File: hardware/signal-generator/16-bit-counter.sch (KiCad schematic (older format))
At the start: 8 parts, among them U1 74HC04, U13 74HC4040, U14 74HC4040, U2 74HC08, U3 74HC08, U4 74HC30

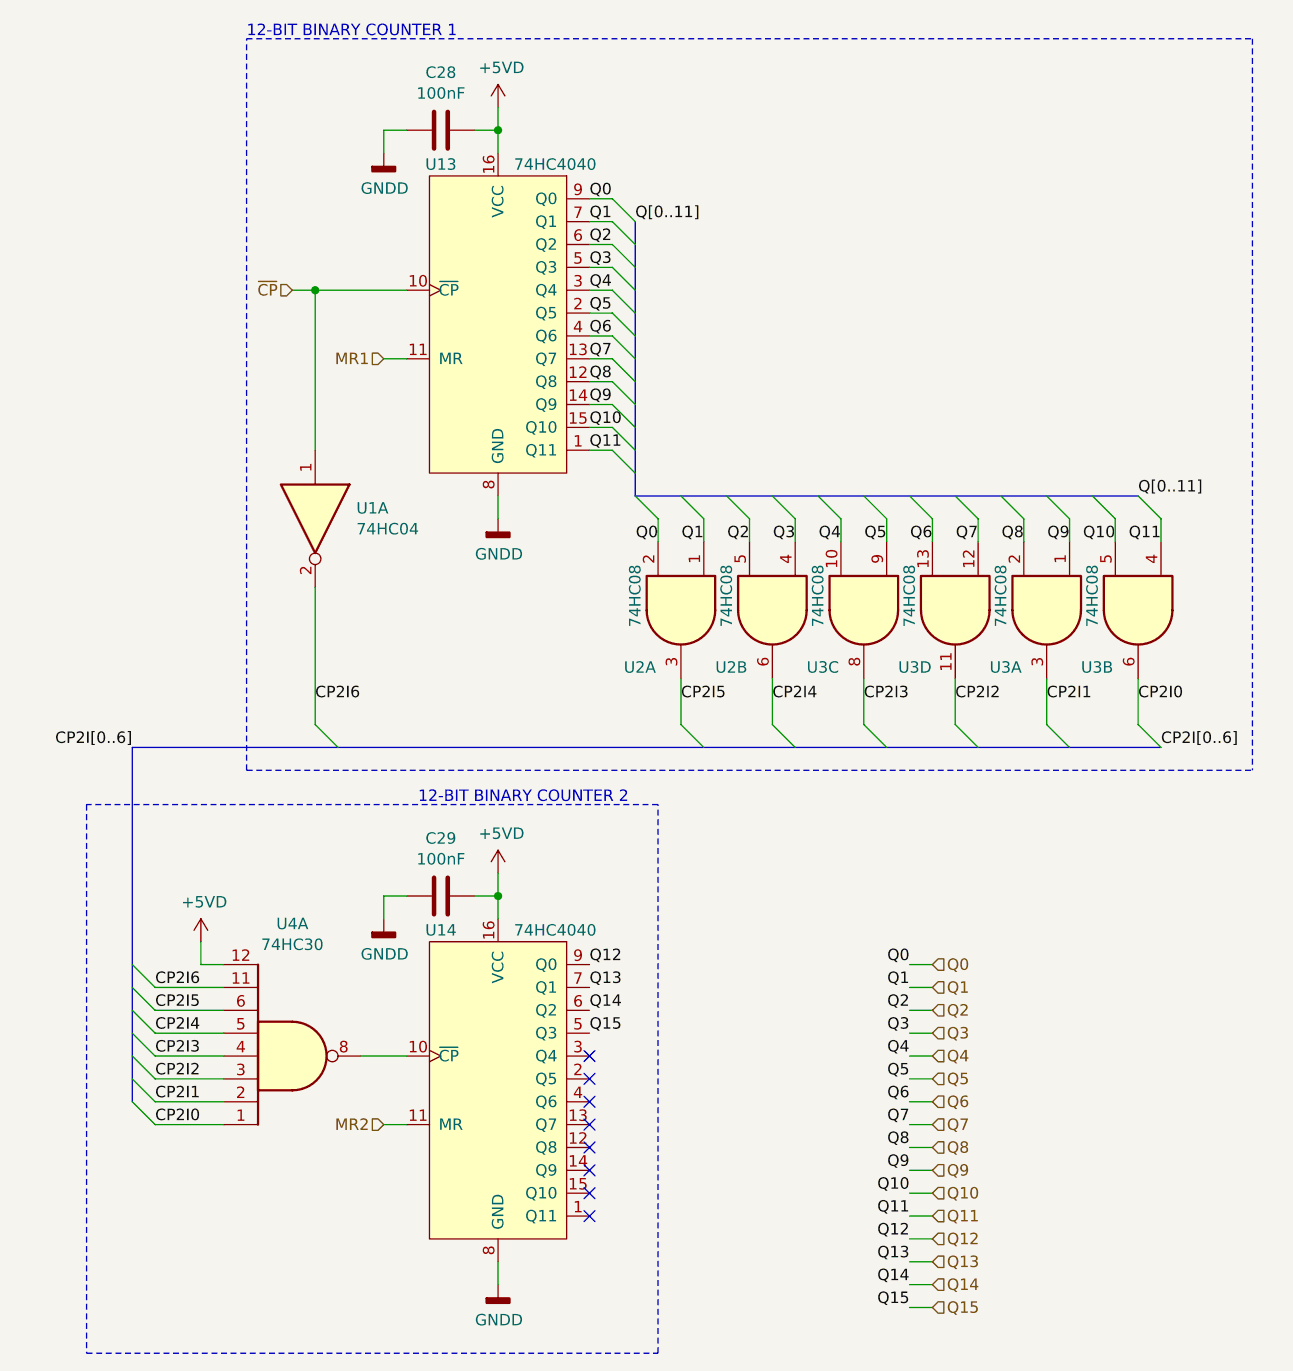
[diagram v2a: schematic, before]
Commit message: [Signal Generator] Complete DDS system layout and routing
All components of the DDS system, as well as their supporting parts, are
laid out compactly on the board.
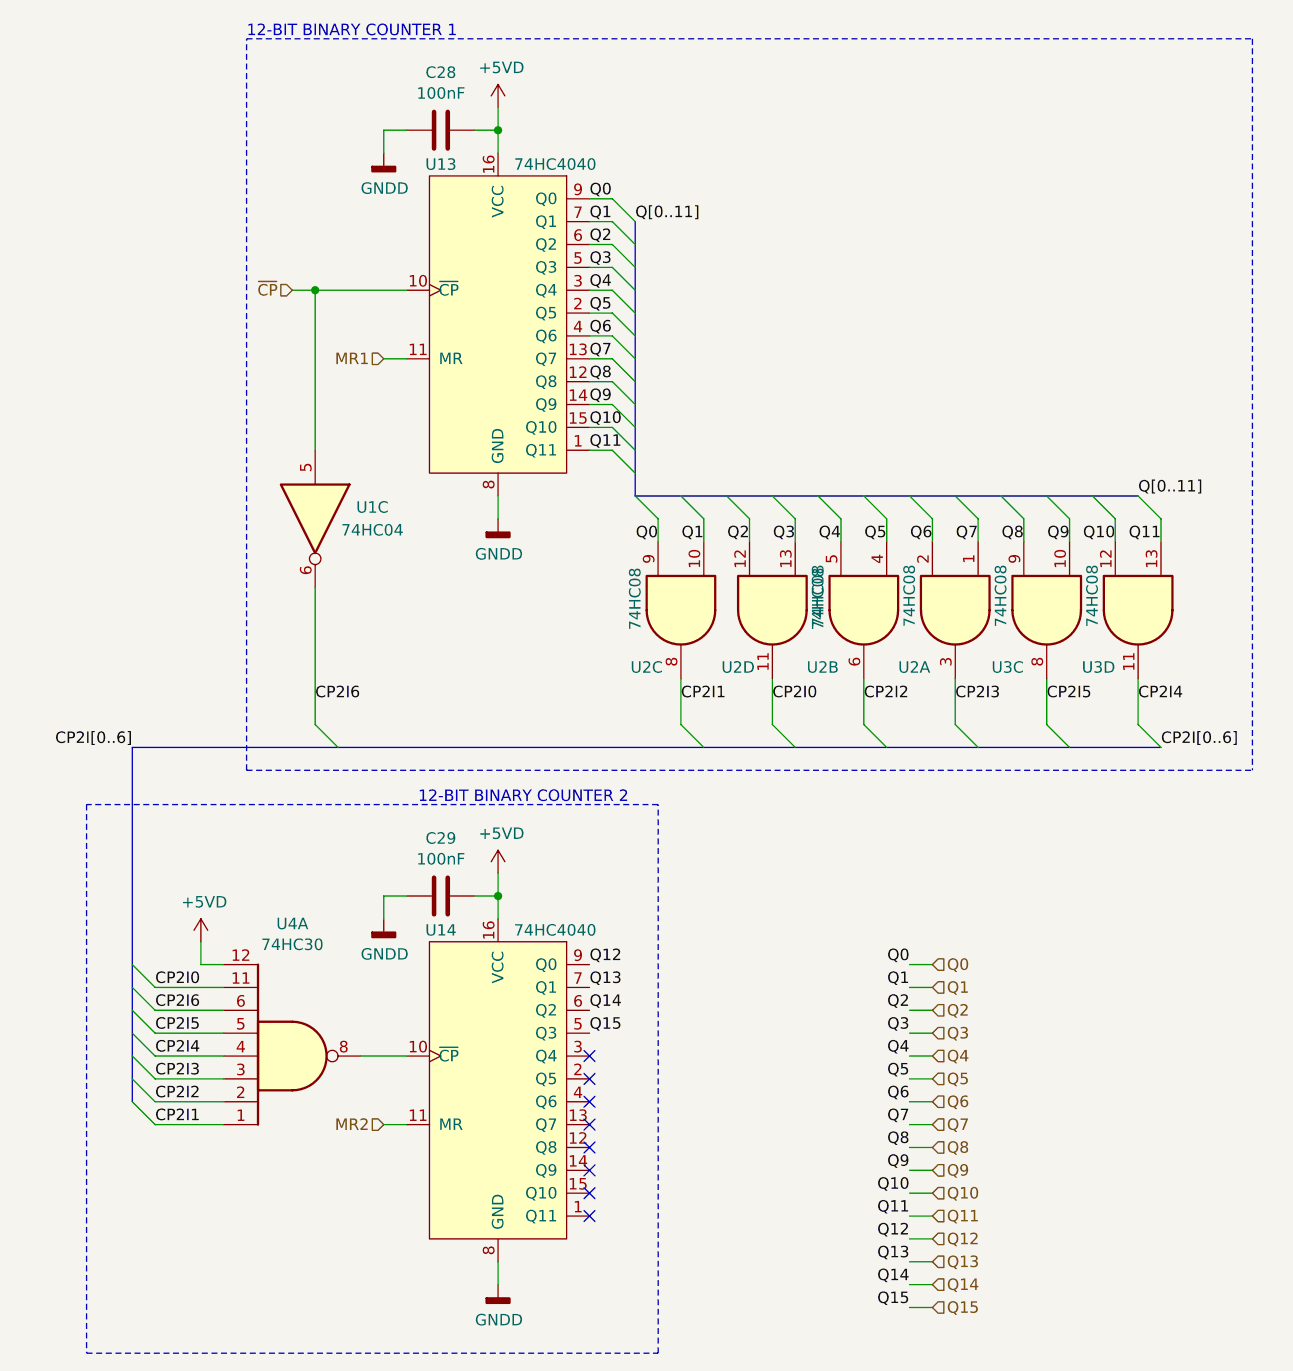
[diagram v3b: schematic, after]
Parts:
- removed U1: 74HC04, Housings_SOIC:SOIC-14_3.9x8.7mm_Pitch1.27mm, symbol 74xx:74HC04
- removed unit 1 of U3
- removed unit 2 of U3
- added U1: 74HC04, Housings_SOIC:SOIC-14_3.9x8.7mm_Pitch1.27mm, symbol 74xx:74HC04
- added unit 4 of U2
- added unit 3 of U2
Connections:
- net CP2I0: now also U4.11, U2.11; no longer U4.1
- net CP2I1: now also U4.1, U2.8; no longer U4.2
- net CP2I2: now also U2.6, U4.2; no longer U3.11, U4.3
- net CP2I3: now also U2.3, U4.3; no longer U3.8, U4.4
- net CP2I4: now also U3.11, U4.4; no longer U2.6, U4.5
- net CP2I5: now also U3.8, U4.5; no longer U2.3, U4.6
- net CP2I6: now also U4.6, U1.6; no longer U4.11
- net Q0: now also U2.9; no longer U2.2
- net Q1: now also U2.10; no longer U2.1
- net Q10: now also U3.12
- net Q11: now also U3.13
- net Q2: now also U2.12; no longer U2.5
- net Q3: now also U2.13; no longer U2.4
- net Q4: now also U2.5; no longer U3.10
- net Q5: now also U2.4; no longer U3.9
- net Q6: now also U2.2; no longer U3.13
- net Q7: now also U2.1; no longer U3.12
- net Q8: now also U3.9
- net Q9: now also U3.10
- net ~CP: now also U1.5
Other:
- moved on the sheet: U2A, U2B, U3C, U3D
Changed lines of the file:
@@
 Sheet 3 5
 Title "Digital Function Generator v2 - DDS 16-bit counter"
-Date "2019-12-02"
+Date "2019-12-26"
 Rev "1"
 Comp "Petar Nikolov"
@@
 Text HLabel 3750 5600 0    50   Input ~ 0
 MR2
+Text Label 2750 5000 0    50   ~ 0
+CP2I0
 Text Label 2750 5600 0    50   ~ 0
-CP2I0
+CP2I1
 Text Label 2750 5500 0    50   ~ 0
-CP2I1
+CP2I2
 Text Label 2750 5400 0    50   ~ 0
-CP2I2
+CP2I3
 Text Label 2750 5300 0    50   ~ 0
-CP2I3
+CP2I4
 Text Label 2750 5200 0    50   ~ 0
-CP2I4
+CP2I5
 Text Label 2750 5100 0    50   ~ 0
-CP2I5
-Text Label 2750 5000 0    50   ~ 0
 CP2I6
 Text Label 2650 3950 2    50   ~ 0
 CP2I[0..6]
+Text Label 5450 3750 0    50   ~ 0
+CP2I0
+Text Label 5050 3750 0    50   ~ 0
+CP2I1
+Text Label 5850 3750 0    50   ~ 0
+CP2I2
+Text Label 6250 3750 0    50   ~ 0
+CP2I3
 Text Label 7050 3750 0    50   ~ 0
-CP2I0
+CP2I4
 Text Label 6650 3750 0    50   ~ 0
-CP2I1
-Text Label 6250 3750 0    50   ~ 0
-CP2I2
-Text Label 5850 3750 0    50   ~ 0
-CP2I3
-Text Label 5450 3750 0    50   ~ 0
-CP2I4
-Text Label 5050 3750 0    50   ~ 0
 CP2I5
 Text Label 3450 3750 0    50   ~ 0
@@
 Text Notes 3900 4200 0    50   ~ 0
 12-BIT BINARY COUNTER 2
-$Comp
-L 74xx:74HC04 U1
-U 1 1 5DBD607E
-P 3450 2950
-F 0 "U1" V 3404 3130 50  0000 L CNN
-F 1 "74HC04" V 3495 3130 50  0000 L CNN
-F 2 "Housings_SOIC:SOIC-14_3.9x8.7mm_Pitch1.27mm" H 3450 2950 50  0001 C CNN
-F 3 "https://assets.nexperia.com/documents/data-sheet/74HC_HCT04.pdf" H 3450 2950 50  0001 C CNN
-	1    3450 2950
-	0    1    1    0
-$EndComp
 Wire Notes Line
 	3150 4050 3150 850
@@
 $Comp
 L ulib_MY_74xx:74HC08 U2
-U 1 1 5DDE88D1
-P 5050 3350
-F 0 "U2" V 5300 3100 50  0000 L CNN
-F 1 "74HC08" H 4850 3150 50  0000 L CNN
-F 2 "Housings_SOIC:SOIC-14_3.9x8.7mm_Pitch1.27mm" H 5050 3300 50  0001 C CNN
-F 3 "https://assets.nexperia.com/documents/data-sheet/74HC_HCT08.pdf" H 5050 3400 50  0001 C CNN
-	1    5050 3350
-	0    1    1    0
-$EndComp
-$Comp
-L ulib_MY_74xx:74HC08 U2
 U 2 1 5DDE89F7
-P 5450 3350
-F 0 "U2" V 5700 3100 50  0000 L CNN
-F 1 "74HC08" H 5250 3150 50  0000 L CNN
-F 2 "Housings_SOIC:SOIC-14_3.9x8.7mm_Pitch1.27mm" H 5450 3300 50  0001 C CNN
-F 3 "https://assets.nexperia.com/documents/data-sheet/74HC_HCT08.pdf" H 5450 3400 50  0001 C CNN
-	2    5450 3350
-	0    1    1    0
-$EndComp
-$Comp
-L ulib_MY_74xx:74HC08 U3
-U 3 1 5DDE8B26
 P 5850 3350
-F 0 "U3" V 6100 3100 50  0000 L CNN
+F 0 "U2" V 6100 3100 50  0000 L CNN
 F 1 "74HC08" H 5650 3150 50  0000 L CNN
 F 2 "Housings_SOIC:SOIC-14_3.9x8.7mm_Pitch1.27mm" H 5850 3300 50  0001 C CNN
 F 3 "https://assets.nexperia.com/documents/data-sheet/74HC_HCT08.pdf" H 5850 3400 50  0001 C CNN
-	3    5850 3350
+	2    5850 3350
 	0    1    1    0
+$EndComp
+$Comp
+L ulib_MY_74xx:74HC08 U3
+U 3 1 5DDE8B26
+P 6650 3350
+F 0 "U3" V 6900 3450 50  0000 L CNN
+F 1 "74HC08" H 6450 3550 50  0000 L CNN
+F 2 "Housings_SOIC:SOIC-14_3.9x8.7mm_Pitch1.27mm" H 6650 3300 50  0001 C CNN
+F 3 "https://assets.nexperia.com/documents/data-sheet/74HC_HCT08.pdf" H 6650 3400 50  0001 C CNN
+	3    6650 3350
+	0    -1   1    0
 $EndComp
 $Comp
 L ulib_MY_74xx:74HC08 U3
 U 4 1 5DDE8C64
+P 7050 3350
+F 0 "U3" V 7300 3450 50  0000 L CNN
+F 1 "74HC08" H 6850 3550 50  0000 L CNN
+F 2 "Housings_SOIC:SOIC-14_3.9x8.7mm_Pitch1.27mm" H 7050 3300 50  0001 C CNN
+F 3 "https://assets.nexperia.com/documents/data-sheet/74HC_HCT08.pdf" H 7050 3400 50  0001 C CNN
+	4    7050 3350
+	0    -1   1    0
+$EndComp
+$Comp
+L ulib_MY_74xx:74HC08 U2
+U 4 1 5E0FAF21
+P 5450 3350
+AR Path="/5DB72CF6/5DBBB708/5E0FAF21" Ref="U2"  Part="4"
+AR Path="/5DE65B3D/5E0FAF21" Ref="U?"  Part="4"
+AR Path="/5E0FAF21" Ref="U?"  Part="4"
+F 0 "U2" V 5700 3500 50  0000 C CNN
+F 1 "74HC08" H 5400 3150 50  0000 C CNN
+F 2 "Housings_SOIC:SOIC-14_3.9x8.7mm_Pitch1.27mm" H 5450 3300 50  0001 C CNN
+F 3 "https://assets.nexperia.com/documents/data-sheet/74HC_HCT08.pdf" H 5450 3400 50  0001 C CNN
+	4    5450 3350
+	0    -1   1    0
+$EndComp
+$Comp
+L ulib_MY_74xx:74HC08 U2
+U 3 1 5E137EE3
+P 5050 3350
+AR Path="/5DB72CF6/5DBBB708/5E137EE3" Ref="U2"  Part="3"
+AR Path="/5DE65B3D/5E137EE3" Ref="U?"  Part="3"
+AR Path="/5E137EE3" Ref="U?"  Part="3"
+F 0 "U2" V 5300 3500 50  0000 C CNN
+F 1 "74HC08" H 5000 3550 50  0000 C CNN
+F 2 "Housings_SOIC:SOIC-14_3.9x8.7mm_Pitch1.27mm" H 5050 3300 50  0001 C CNN
+F 3 "https://assets.nexperia.com/documents/data-sheet/74HC_HCT08.pdf" H 5050 3400 50  0001 C CNN
+	3    5050 3350
+	0    -1   1    0
+$EndComp
+$Comp
+L ulib_MY_74xx:74HC08 U2
+U 1 1 5DDE88D1
 P 6250 3350
-F 0 "U3" V 6500 3100 50  0000 L CNN
+F 0 "U2" V 6500 3100 50  0000 L CNN
 F 1 "74HC08" H 6050 3150 50  0000 L CNN
 F 2 "Housings_SOIC:SOIC-14_3.9x8.7mm_Pitch1.27mm" H 6250 3300 50  0001 C CNN
 F 3 "https://assets.nexperia.com/documents/data-sheet/74HC_HCT08.pdf" H 6250 3400 50  0001 C CNN
-	4    6250 3350
+	1    6250 3350
 	0    1    1    0
 $EndComp
 $Comp
-L ulib_MY_74xx:74HC08 U3
-U 1 1 5DDE8DB3
-P 6650 3350
-F 0 "U3" V 6900 3100 50  0000 L CNN
-F 1 "74HC08" H 6450 3150 50  0000 L CNN
-F 2 "Housings_SOIC:SOIC-14_3.9x8.7mm_Pitch1.27mm" H 6650 3300 50  0001 C CNN
-F 3 "https://assets.nexperia.com/documents/data-sheet/74HC_HCT08.pdf" H 6650 3400 50  0001 C CNN
-	1    6650 3350
+L 74xx:74HC04 U?
+U 3 1 5E4488E7
+P 3450 2950
+AR Path="/5E4488E7" Ref="U?"  Part="3"
+AR Path="/5DB72CF6/5DBBB708/5E4488E7" Ref="U1"  Part="3"
+F 0 "U1" V 3400 3200 50  0000 C CNN
+F 1 "74HC04" V 3500 3200 50  0000 C CNN
+F 2 "Housings_SOIC:SOIC-14_3.9x8.7mm_Pitch1.27mm" H 3450 2950 50  0001 C CNN
+F 3 "https://assets.nexperia.com/documents/data-sheet/74HC_HCT04.pdf" H 3450 2950 50  0001 C CNN
+	3    3450 2950
 	0    1    1    0
 $EndComp
-$Comp
-L ulib_MY_74xx:74HC08 U3
-U 2 1 5DDE8F14
-P 7050 3350
-F 0 "U3" V 7300 3100 50  0000 L CNN
-F 1 "74HC08" H 6850 3150 50  0000 L CNN
-F 2 "Housings_SOIC:SOIC-14_3.9x8.7mm_Pitch1.27mm" H 7050 3300 50  0001 C CNN
-F 3 "https://assets.nexperia.com/documents/data-sheet/74HC_HCT08.pdf" H 7050 3400 50  0001 C CNN
-	2    7050 3350
-	0    1    1    0
-$EndComp
